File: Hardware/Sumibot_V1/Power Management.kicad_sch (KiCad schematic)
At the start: 21 parts, among them Q2 DMG2301L, Q3 DMG2301L, Q4 DMG2301L, SW3 SW_SPDT, U5 MCP73831-3-OT, U6 AP2112K-3.3

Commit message: Incluyendo toggle
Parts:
- added Q? (x2): (no value), symbol Transistor_FET:IRF7343PBF
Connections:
- new net: Q?.7 (D), Q?.8 (D)
- new net: Q?.5 (D), Q?.6 (D)
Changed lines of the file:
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@@
     (pin "1")
+  )
+  (symbol (lib_id "Transistor_FET:IRF7343PBF") (at 71.12 111.76 0) (unit 1)
+    (in_bom yes) (on_board yes) (fields_autoplaced)
+    (property "Reference" "Q?" (id 0) (at 77.47 110.4899 0)
+      (effects (font (size 1.27 1.27)) (justify left))
+    )
+    (property "Value" "" (id 1) (at 77.47 113.0299 0)
+      (effects (font (size 1.27 1.27)) (justify left))
+    )
+    (property "Footprint" "" (id 2) (at 76.2 113.665 0)
+      (effects (font (size 1.27 1.27)) (justify left) hide)
+    )
+    (property "Datasheet" "http://www.irf.com/product-info/datasheets/data/irf7343ipbf.pdf" (id 3) (at 73.66 111.76 0)
+      (effects (font (size 1.27 1.27)) (justify left) hide)
+    )
+    (pin "1")
+    (pin "2")
+    (pin "7")
+    (pin "8")
+    (pin "3")
+    (pin "4")
+    (pin "5")
+    (pin "6")
   )
   (symbol (lib_id "Device:R_Small_US") (at 159.766 56.769 0) (unit 1)
@@
     (pin "1")
   )
+  (symbol (lib_id "Transistor_FET:IRF7343PBF") (at 73.66 132.08 0) (unit 2)
+    (in_bom yes) (on_board yes) (fields_autoplaced)
+    (property "Reference" "Q?" (id 0) (at 80.01 130.8099 0)
+      (effects (font (size 1.27 1.27)) (justify left))
+    )
+    (property "Value" "" (id 1) (at 80.01 133.3499 0)
+      (effects (font (size 1.27 1.27)) (justify left))
+    )
+    (property "Footprint" "" (id 2) (at 78.74 133.985 0)
+      (effects (font (size 1.27 1.27)) (justify left) hide)
+    )
+    (property "Datasheet" "http://www.irf.com/product-info/datasheets/data/irf7343ipbf.pdf" (id 3) (at 76.2 132.08 0)
+      (effects (font (size 1.27 1.27)) (justify left) hide)
+    )
+    (pin "1")
+    (pin "2")
+    (pin "7")
+    (pin "8")
+    (pin "3")
+    (pin "4")
+    (pin "5")
+    (pin "6")
+  )
   (symbol (lib_id "power:GND") (at 171.196 62.23 0) (unit 1)

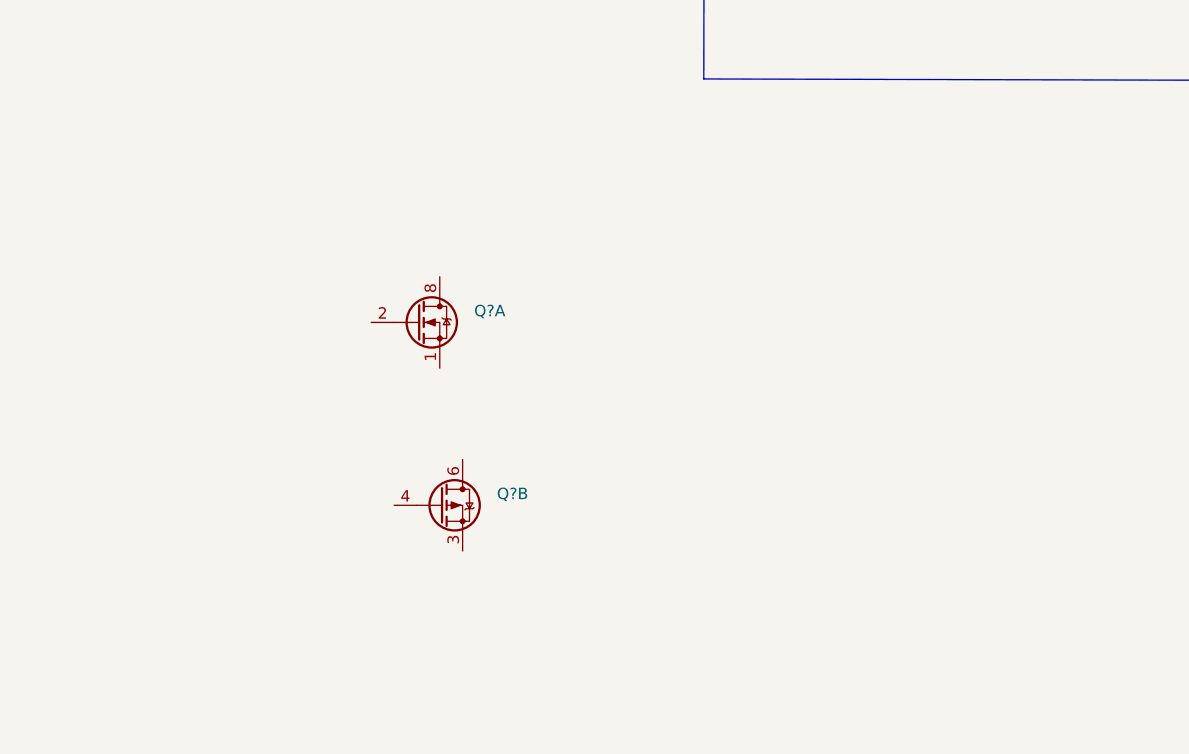
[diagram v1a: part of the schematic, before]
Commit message: Circuito toggle, diagrama kicad
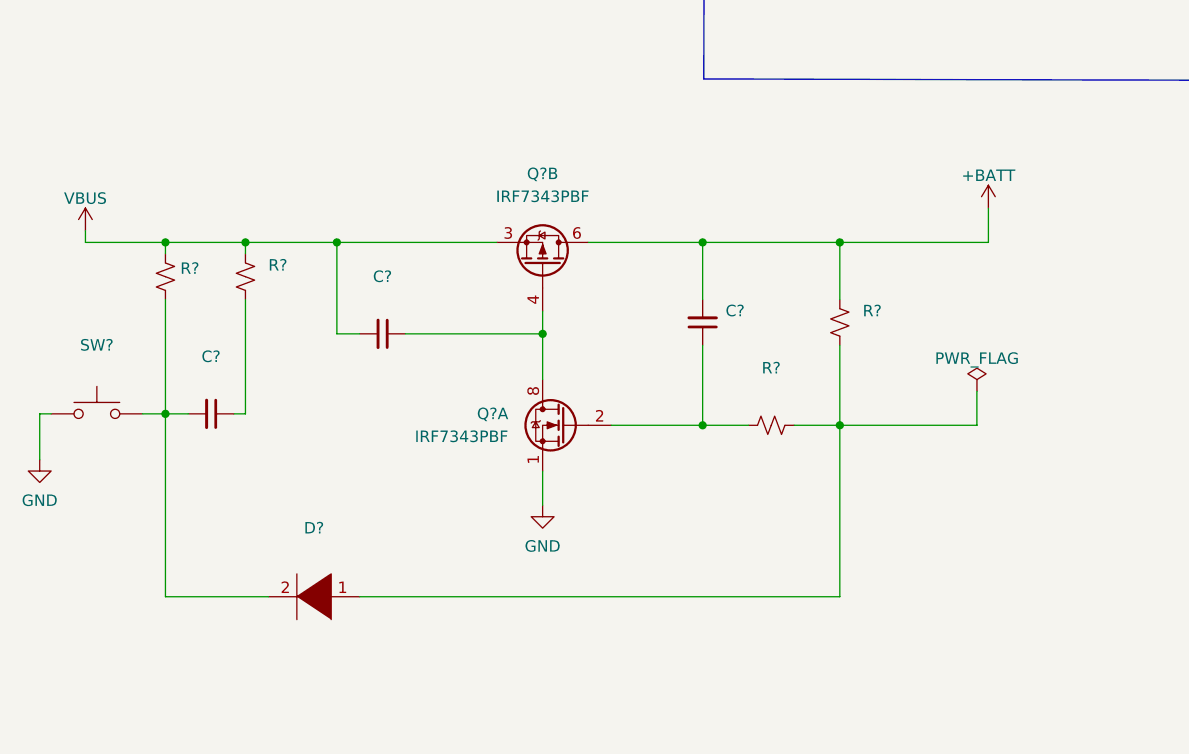
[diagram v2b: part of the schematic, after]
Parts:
- added C? (x3): (no value), Capacitor_SMD:C_0805_2012Metric, symbol Device:C_Small
- added D?: (no value), symbol pspice:DIODE
- added R? (x3): (no value), Resistor_SMD:R_0805_2012Metric, symbol Device:R_Small_US
- added R?: (no value), symbol Device:R_Small_US
- added SW?: (no value), symbol Switch:SW_Push
- Q? (x2): value (none) -> IRF7343PBF; footprint (none) -> Package_SO:SOIC-8_3.9x4.9mm_P1.27mm
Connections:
- net +BATT: now also Q?.5 (D), Q?.6 (D), C?.2, R?.1
- net GND: now also Q?.1 (S), SW?.1
- net VBUS: now also Q?.3 (1), C?.2, R?.1, R?.1
- net at Q?.2 (G): now also C?.1, R?.2
- net at Q?.7 (D), Q?.8 (D): now also Q?.4 (G), C?.1
- new net: D?.1 (K), R?.1, R?.2
- new net: C?.1, R?.2
- new net: C?.2, D?.2 (A), R?.2, SW?.2
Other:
- moved on the sheet: Q?A, Q?B

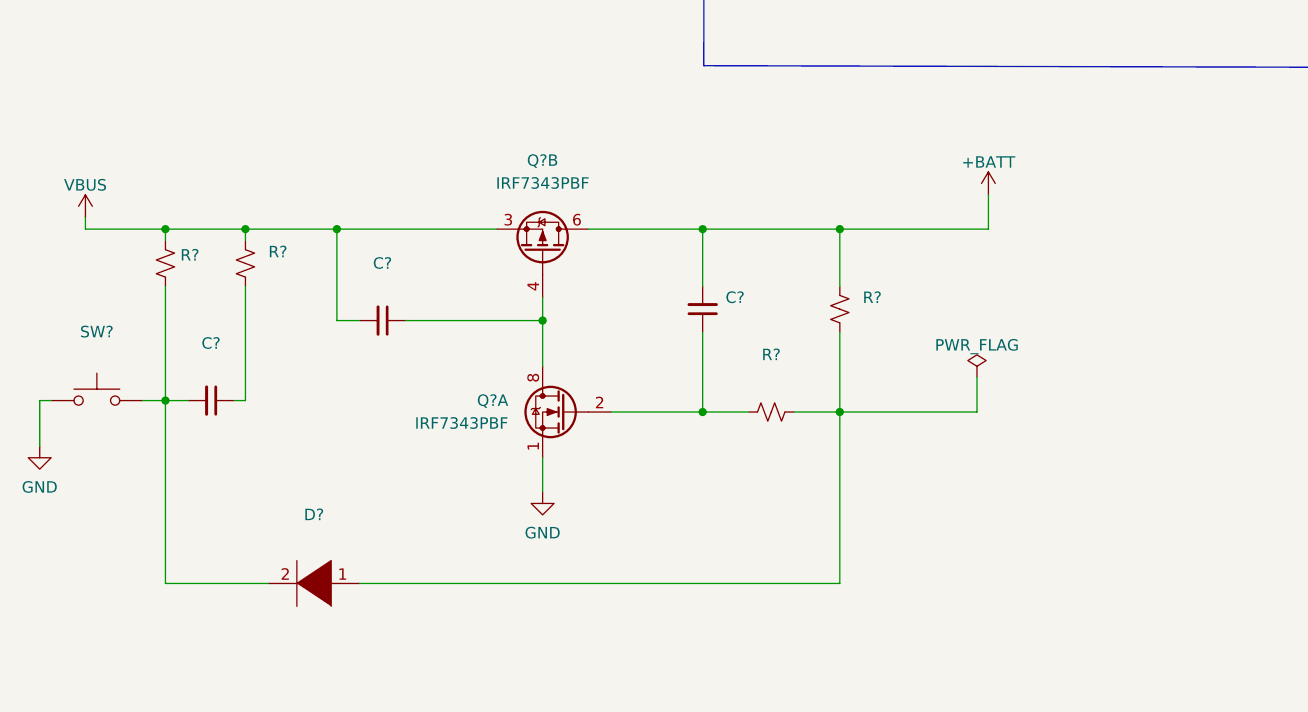
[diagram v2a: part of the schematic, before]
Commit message: implementó on/off toggle switch
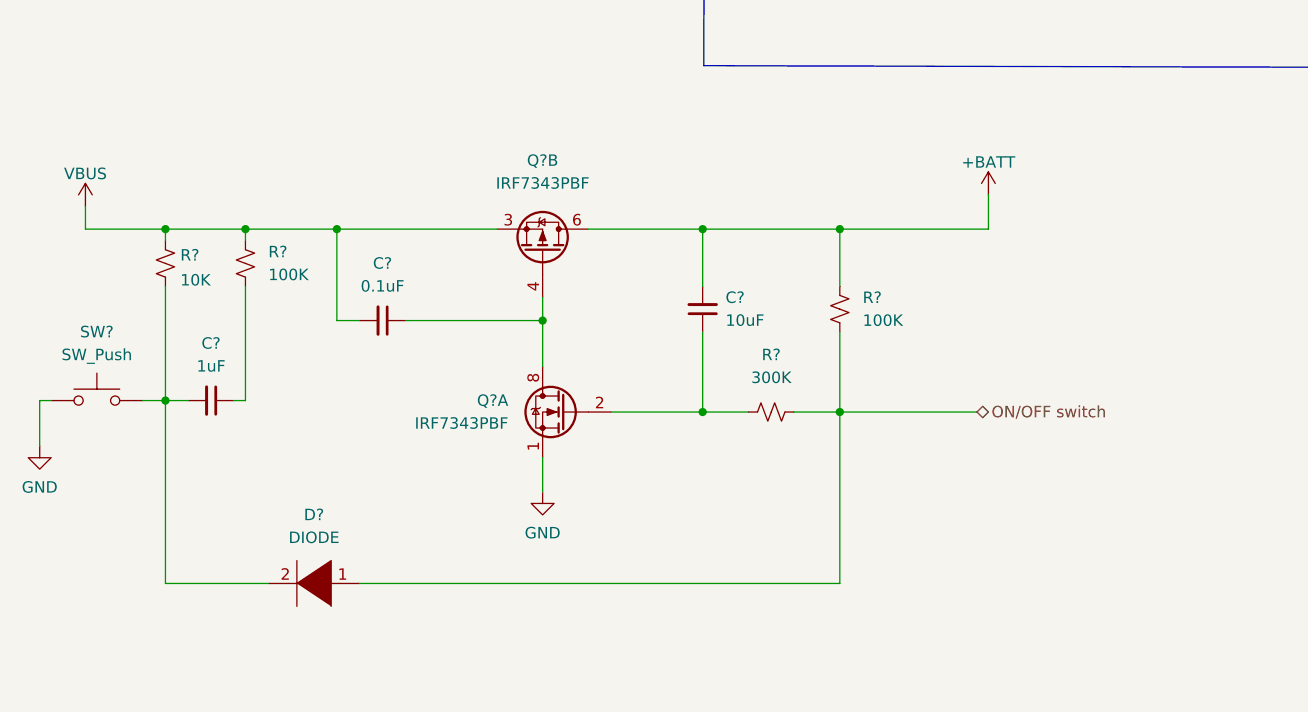
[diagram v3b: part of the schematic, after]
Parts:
- C?: value (none) -> 0.1uF
- C?: value (none) -> 10uF
- C?: value (none) -> 1uF
- D?: value (none) -> DIODE; footprint (none) -> Diode_SMD:D_0201_0603Metric
- R? (x2): value (none) -> 100K
- R?: value (none) -> 300K
- R?: value (none) -> 10K; footprint (none) -> Resistor_SMD:R_0805_2012Metric
- SW?: value (none) -> SW_Push
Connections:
- net ON/OFF switch: now reaches D?.1 (K), R?.1, R?.2
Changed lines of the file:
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@@
     (stroke (width 0) (type default) (color 0 0 0 0))
   )
-  (wire (pts (xy 133.35 123.19) (xy 118.11 123.19))
+  (wire (pts (xy 118.11 123.19) (xy 133.35 123.19))
     (stroke (width 0) (type default) (color 0 0 0 0))
   )
@@
     (stroke (width 0) (type default) (color 0 0 0 0))
   )
-  (wire (pts (xy 34.29 101.6) (xy 34.29 102.87))
+  (wire (pts (xy 34.29 100.33) (xy 34.29 102.87))
     (stroke (width 0) (type default) (color 0 0 0 0))
   )
@@
   )
   (wire (pts (xy 43.18 142.24) (xy 54.61 142.24))
-    (stroke (width 0) (type default) (color 0 0 0 0))
-  )
-  (wire (pts (xy 133.35 119.38) (xy 133.35 123.19))
     (stroke (width 0) (type default) (color 0 0 0 0))
   )
@@
   )
   (hierarchical_label "BattMeter" (shape output) (at 190.754 52.959 0)
+    (effects (font (size 1.27 1.27)) (justify left))
+  )
+  (hierarchical_label "ON{slash}OFF switch" (shape bidirectional) (at 133.35 123.19 0)
     (effects (font (size 1.27 1.27)) (justify left))
   )
@@
     (in_bom yes) (on_board yes) (fields_autoplaced)
     (property "Reference" "C?" (id 0) (at 67.3036 106.68 90))
-    (property "Value" "" (id 1) (at 67.3036 109.22 90))
+    (property "Value" "0.1uF" (id 1) (at 67.3036 109.22 90))
     (property "Footprint" "Capacitor_SMD:C_0805_2012Metric" (id 2) (at 67.31 113.03 0)
       (effects (font (size 1.27 1.27)) hide)
@@
       (effects (font (size 1.27 1.27)) (justify left))
     )
-    (property "Value" "" (id 1) (at 120.65 113.0299 0)
+    (property "Value" "100K" (id 1) (at 120.65 113.0299 0)
       (effects (font (size 1.27 1.27)) (justify left))
     )
@@
       (effects (font (size 1.27 1.27)) (justify right))
     )
-    (property "Value" "" (id 1) (at 105.41 113.0235 0)
+    (property "Value" "10uF" (id 1) (at 105.41 113.0235 0)
       (effects (font (size 1.27 1.27)) (justify right))
     )
@@
     (pin "1")
   )
-  (symbol (lib_id "power:VBUS") (at 34.29 101.6 0) (unit 1)
-    (in_bom yes) (on_board yes) (fields_autoplaced)
-    (property "Reference" "#PWR?" (id 0) (at 34.29 105.41 0)
-      (effects (font (size 1.27 1.27)) hide)
-    )
-    (property "Value" "VBUS" (id 1) (at 34.29 97.9955 0))
-    (property "Footprint" "" (id 2) (at 34.29 101.6 0)
-      (effects (font (size 1.27 1.27)) hide)
-    )
-    (property "Datasheet" "" (id 3) (at 34.29 101.6 0)
+  (symbol (lib_id "power:VBUS") (at 34.29 100.33 0) (unit 1)
+    (in_bom yes) (on_board yes) (fields_autoplaced)
+    (property "Reference" "#PWR?" (id 0) (at 34.29 104.14 0)
+      (effects (font (size 1.27 1.27)) hide)
+    )
+    (property "Value" "VBUS" (id 1) (at 34.29 96.7255 0))
+    (property "Footprint" "" (id 2) (at 34.29 100.33 0)
+      (effects (font (size 1.27 1.27)) hide)
+    )
+    (property "Datasheet" "" (id 3) (at 34.29 100.33 0)
       (effects (font (size 1.27 1.27)) hide)
     )
@@
     (in_bom yes) (on_board yes) (fields_autoplaced)
     (property "Reference" "C?" (id 0) (at 48.2536 115.57 90))
-    (property "Value" "" (id 1) (at 48.2536 118.11 90))
+    (property "Value" "1uF" (id 1) (at 48.2536 118.11 90))
     (property "Footprint" "Capacitor_SMD:C_0805_2012Metric" (id 2) (at 48.26 121.92 0)
       (effects (font (size 1.27 1.27)) hide)
@@
     (pin "1")
   )
-  (symbol (lib_id "power:PWR_FLAG") (at 133.35 119.38 0) (mirror y) (unit 1)
-    (in_bom yes) (on_board yes) (fields_autoplaced)
-    (property "Reference" "#FLG?" (id 0) (at 133.35 117.475 0)
-      (effects (font (size 1.27 1.27)) hide)
-    )
-    (property "Value" "PWR_FLAG" (id 1) (at 133.35 115.7755 0))
-    (property "Footprint" "" (id 2) (at 133.35 119.38 0)
-      (effects (font (size 1.27 1.27)) hide)
-    )
-    (property "Datasheet" "~" (id 3) (at 133.35 119.38 0)
-      (effects (font (size 1.27 1.27)) hide)
-    )
-    (pin "1")
-  )
   (symbol (lib_id "Device:R_Small_US") (at 52.07 106.68 0) (unit 1)
     (in_bom yes) (on_board yes) (fields_autoplaced)
@@
       (effects (font (size 1.27 1.27)) (justify left))
     )
-    (property "Value" "" (id 1) (at 54.61 107.9499 0)
+    (property "Value" "100K" (id 1) (at 54.61 107.9499 0)
       (effects (font (size 1.27 1.27)) (justify left))
     )
@@
     (in_bom yes) (on_board yes) (fields_autoplaced)
     (property "Reference" "SW?" (id 0) (at 35.56 114.3 0))
-    (property "Value" "" (id 1) (at 35.56 116.84 0))
+    (property "Value" "SW_Push" (id 1) (at 35.56 116.84 0))
     (property "Footprint" "" (id 2) (at 35.56 116.84 0)
       (effects (font (size 1.27 1.27)) hide)
@@
     (in_bom yes) (on_board yes) (fields_autoplaced)
     (property "Reference" "D?" (id 0) (at 59.69 134.62 0))
-    (property "Value" "" (id 1) (at 59.69 137.16 0))
-    (property "Footprint" "" (id 2) (at 59.69 142.24 0)
+    (property "Value" "DIODE" (id 1) (at 59.69 137.16 0))
+    (property "Footprint" "Diode_SMD:D_0201_0603Metric" (id 2) (at 59.69 142.24 0)
       (effects (font (size 1.27 1.27)) hide)
     )
@@
     (in_bom yes) (on_board yes) (fields_autoplaced)
     (property "Reference" "R?" (id 0) (at 110.49 116.84 90))
-    (property "Value" "" (id 1) (at 110.49 119.38 90))
+    (property "Value" "300K" (id 1) (at 110.49 119.38 90))
     (property "Footprint" "Resistor_SMD:R_0805_2012Metric" (id 2) (at 110.49 123.19 0)
       (effects (font (size 1.27 1.27)) hide)
@@
       (effects (font (size 1.27 1.27)) (justify left))
     )
-    (property "Value" "" (id 1) (at 44.831 108.5466 0)
-      (effects (font (size 1.27 1.27)) (justify left))
-    )
-    (property "Footprint" "" (id 2) (at 43.18 106.68 0)
-      (effects (font (size 1.27 1.27)) hide)
-    )
+    (property "Value" "10K" (id 1) (at 44.831 108.5466 0)
+      (effects (font (size 1.27 1.27)) (justify left))
+    )
+    (property "Footprint" "Resistor_SMD:R_0805_2012Metric" (id 2) (at 43.18 106.68 0)
+      (effects (font (size 1.27 1.27)) hide)
+    )
